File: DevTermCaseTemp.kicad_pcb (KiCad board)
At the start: 2 copper layers, 98.2 x 77 mm, 1 part, among them J1 miniPCIe

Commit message: in production. good luck!
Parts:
- added C1: 10uF, Capacitor_SMD:C_0805_2012Metric, B.Cu at (106.1, 81.5)
- added C10: 1uF, Capacitor_SMD:C_0805_2012Metric, B.Cu at (135.1, 94.3)
- added C11: 100nF, Capacitor_SMD:C_0805_2012Metric, B.Cu at (133.1, 94.3)
- added C12: 20pF, Capacitor_SMD:C_0805_2012Metric, B.Cu at (139.2, 109.2)
- added C13: 20pF, Capacitor_SMD:C_0805_2012Metric, B.Cu at (139.2, 101.6)
- added C14: 100nF, Capacitor_SMD:C_0805_2012Metric, B.Cu at (170.4, 122.9)
- added C15: 100nF, Capacitor_SMD:C_0805_2012Metric, B.Cu at (128.8, 91.4)
- added C16: 100nF, Capacitor_SMD:C_0805_2012Metric, B.Cu at (150.1, 121.2)
- added C17: 100nF, Capacitor_SMD:C_0805_2012Metric, B.Cu at (158.8, 122.4)
- added C2: 1uF, Capacitor_SMD:C_0805_2012Metric, B.Cu at (141.0, 97.8)
- added C3: 100nF, Capacitor_SMD:C_0805_2012Metric, B.Cu at (125.2, 116.3)
- added C4: 10uF, Capacitor_SMD:C_0805_2012Metric, B.Cu at (111.8, 118.6)
- added C5: 10uF, Capacitor_SMD:C_0805_2012Metric, B.Cu at (122.6, 116.1)
- added C6: 100nF, Capacitor_SMD:C_0805_2012Metric, B.Cu at (124.0, 103.1)
- added C7: 100nF, Capacitor_SMD:C_0805_2012Metric, B.Cu at (124.0, 99.3)
- added C8: 100nF, Capacitor_SMD:C_0805_2012Metric, B.Cu at (129.0, 96.0)
- added C9: 1uF, Capacitor_SMD:C_0805_2012Metric, B.Cu at (127.0, 96.0)
- added D1: ESD, Diode_SMD:D_SOD-323, B.Cu at (178.7, 96.5)
- added D10: ESD, Diode_SMD:D_SOD-323, B.Cu at (183.1, 103.1)
- added D11: ESD, Diode_SMD:D_SOD-323, B.Cu at (183.2, 100.1)
- added D12: ESD, Diode_SMD:D_SOD-323, B.Cu at (109.8, 66.6)
- added D13: ESD, Diode_SMD:D_SOD-323, B.Cu at (109.8, 69.9)
- added D14: ESD, Diode_SMD:D_SOD-323, B.Cu at (166.6, 79.2)
- added D15: ESD, Diode_SMD:D_SOD-323, B.Cu at (169.2, 79.2)
- added D16: ESD, Diode_SMD:D_SOD-323, B.Cu at (111.8, 66.6)
- added D17: ESD, Diode_SMD:D_SOD-323, B.Cu at (111.8, 69.9)
- added D18: ESD, Diode_SMD:D_SOD-323, B.Cu at (164.1, 79.2)
- added D19: ESD, Diode_SMD:D_SOD-323, B.Cu at (161.5, 79.2)
- added D2: ESD, Diode_SMD:D_SOD-323, B.Cu at (175.0, 80.4)
- added D3: ESD, Diode_SMD:D_SOD-323, B.Cu at (178.7, 98.5)
- added D4: ESD, Diode_SMD:D_SOD-323, B.Cu at (174.8, 119.9)
- added D5: ESD, Diode_SMD:D_SOD-323, B.Cu at (178.7, 103.7)
- added D6: ESD, Diode_SMD:D_SOD-323, B.Cu at (174.9, 117.6)
- added D7: LED, LED_SMD:LED_0603_1608Metric, B.Cu at (172.3, 135.9)
- added D8: LED, LED_SMD:LED_0603_1608Metric, B.Cu at (168.5, 135.9)
- added D9: ESD, Diode_SMD:D_SOD-323, B.Cu at (183.2, 97.1)
- added FB1: FerriteBead, Capacitor_SMD:C_0805_2012Metric, B.Cu at (131.8, 116.1)
- added FB2: FerriteBead, Capacitor_SMD:C_0805_2012Metric, B.Cu at (124.0, 107.7)
- added H1: MountingHole_Pad, MountingHole:MountingHole_2.7mm_M2.5_DIN965_Pad, F.Cu at (147.4, 84.5)
- added H2: MountingHole_Pad, MountingHole:MountingHole_2.7mm_M2.5_DIN965_Pad, F.Cu at (172.5, 84.5)
- added H3: MountingHole_Pad, MountingHole:MountingHole_2.7mm_M2.5_DIN965_Pad, F.Cu at (172.5, 113.6)
- added J1: USB_A, Connector_USB:USB_A_CONNFLY_DS1095-WNR0, F.Cu at (179.1, 90.3)
- added J3: USB_A, Connector_USB:USB_A_CONNFLY_DS1095-WNR0, F.Cu at (179.1, 117.3)
- added J4: USB_B_Micro, Connector_USB:USB_Micro-B_Amphenol_10118194_Horizontal, B.Cu at (188.1, 100.3)
- added J5: JBAT, Connector_PinSocket_2.00mm:PinSocket_1x02_P2.00mm_Horizontal, B.Cu at (147.8, 132.2)
- added J6: Conn_01x04, Connector_PinSocket_2.00mm:PinSocket_1x04_P2.00mm_Horizontal, B.Cu at (172.9, 74.7)
- added J7: DevTermSpeaker, devterm-ext-outline:DevTerm-Speaker, F.Cu at (171.1, 126.7)
- added J8: DevTermSpeaker, devterm-ext-outline:DevTerm-Speaker, F.Cu at (116.8, 126.7)
- added J9: Conn_02x22_Odd_Even, devterm-ext-outline:C64_expansion_2x22_socket, B.Cu at (169.2, 72.1)
- added JP1: A2, Connector_PinHeader_2.54mm:PinHeader_1x03_P2.54mm_Horizontal, B.Cu at (118.6, 124.2)
- added JP2: A1, Connector_PinHeader_2.54mm:PinHeader_1x03_P2.54mm_Horizontal, B.Cu at (128.8, 124.2)
- added JP3: A0, Connector_PinHeader_2.54mm:PinHeader_1x03_P2.54mm_Horizontal, B.Cu at (138.9, 124.2)
- added R1: 30K, Resistor_SMD:R_0805_2012Metric, B.Cu at (126.2, 113.5)
- added R10: 10K, Resistor_SMD:R_0805_2012Metric, B.Cu at (113.5, 111.5)
- added R11: 6.8K/1%, Resistor_SMD:R_0805_2012Metric, B.Cu at (109.2, 114.6)
- added R12: 1K, Resistor_SMD:R_0805_2012Metric, B.Cu at (176.1, 129.3)
- added R13: 15K, Resistor_SMD:R_0805_2012Metric, B.Cu at (124.5, 91.4)
- added R14: 1K, Resistor_SMD:R_0805_2012Metric, B.Cu at (165.4, 129.3)
- added R15: 100K, Resistor_SMD:R_0805_2012Metric, B.Cu at (113.0, 123.2)
- added R16: 100K, Resistor_SMD:R_0805_2012Metric, B.Cu at (110.5, 123.2)
- added R17: 1K, Resistor_SMD:R_0805_2012Metric, B.Cu at (168.5, 131.2)
- added R18: 1K, Resistor_SMD:R_0805_2012Metric, B.Cu at (172.3, 131.2)
- added R19: 100K, Resistor_SMD:R_0805_2012Metric, B.Cu at (114.8, 78.5)
- added R2: 680R/1%, Resistor_SMD:R_0805_2012Metric, B.Cu at (131.8, 113.3)
- added R3: 100K, Resistor_SMD:R_0805_2012Metric, B.Cu at (138.6, 94.2)
- added R4: 10K, Resistor_SMD:R_0805_2012Metric, B.Cu at (140.6, 94.2)
- added R5: 10K, Resistor_SMD:R_0805_2012Metric, B.Cu at (107.2, 73.7)
- added R6: 100K, Resistor_SMD:R_0805_2012Metric, B.Cu at (130.3, 111.3)
- added R7: 6.8K/1%, Resistor_SMD:R_0805_2012Metric, B.Cu at (104.0, 77.9)
- added R8: 47K, Resistor_SMD:R_0805_2012Metric, B.Cu at (134.6, 97.9)
- added R9: 30K, Resistor_SMD:R_0805_2012Metric, B.Cu at (129.8, 116.1)
- added REF**: mpcie-silk-back, devterm-ext-outline:mpcie-silk-back, B.Cu at (94.3, 98.0)
- added REF**: turbo_fan_3505, devterm-ext-outline:turbo_fan_3505, B.Cu at (180.0, 99.1)
- added SW1: SW_DIP_x02, Button_Switch_SMD:SW_DIP_SPSTx02_Slide_6.7x6.64mm_W6.73mm_P2.54mm_LowProfile_JPin, B.Cu at (112.0, 129.8)
- added U1: GL850G, GL850G:SSOP28, B.Cu at (130.6, 105.7)
- added U10: 4052, Package_SO:SOIC-16_3.9x9.9mm_P1.27mm, B.Cu at (104.9, 95.2)
- added U11: 4052, Package_SO:SOIC-16_3.9x9.9mm_P1.27mm, B.Cu at (118.1, 95.2)
- added U12: TXS0102DCU, Package_SO:VSSOP-8_2.3x2mm_P0.5mm, B.Cu at (153.9, 120.4)
- added U2: SY6280, SY6280:SOT23-5P95_285X100L45X40N, B.Cu at (107.5, 77.6)
- added U3: SY6280, SY6280:SOT23-5P95_285X100L45X40N, B.Cu at (113.3, 114.8)
- added U4: DS1307+, devterm-ext-outline:SOIC-8, B.Cu at (154.7, 129.3)
- added U5: MCP23008-xSS, Package_SO:SOIC-20W_7.5x12.8mm_P1.27mm, B.Cu at (130.3, 83.3)
- added U6: CH340N, Package_SO:SOP-8_3.9x4.9mm_P1.27mm, B.Cu at (170.4, 126.7)
- added U7: 4052, Package_SO:SOIC-16_3.9x9.9mm_P1.27mm, B.Cu at (138.2, 116.8)
- added U8: 4052, Package_SO:SOIC-16_3.9x9.9mm_P1.27mm, B.Cu at (104.9, 107.2)
- added U9: gp7101, Package_SO:SOP-8_3.9x4.9mm_P1.27mm, B.Cu at (185.9, 75.2)
- added Y1: 12MHz, Crystal:Crystal_SMD_3225-4Pin_3.2x2.5mm_HandSoldering, B.Cu at (139.2, 105.4)
- added Y2: 32.768KHz, Crystal:Crystal_DS26_D2.0mm_L6.0mm_Horizontal, B.Cu at (158.8, 132.3)
- J2: renamed from J1; value miniPCIe -> EXT_miniPCIe
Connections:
- net /CAM_D2_N renamed /CAM2.D-
- net /CAM_D2_P renamed /CAM2.D+
- net /CAM_D3_N renamed /CAM3.D-
- net /CAM_D3_P renamed /CAM3.D+
- J2 pad 13: /USB4_D_P -> /USB4.D+
- J2 pad 15: /USB4_D_N -> /USB4.D-
- J2 pad 17: unconnected-(J1-Pad17) -> +3.3V
- J2 pad 19: unconnected-(J1-Pad19) -> +3.3V
- J2 pad 35: /CAM_C_P -> /CAM.C+
- J2 pad 37: /CAM_C_N -> /CAM.C-
- J2 pad 41: /CAM_D1_P -> /CAM1.D+
- J2 pad 43: /CAM_D1_N -> /CAM1.D-
- J2 pad 45: unconnected-(J1-Pad45) -> GND
- J2 pad 47: unconnected-(J1-Pad47) -> /CAM0.D+
- J2 pad 49: unconnected-(J1-Pad49) -> /CAM0.D-
- J2 pad 51: unconnected-(J1-Pad51) -> GND
- J2 pad 7: /USB3_D_P -> /USB3.D+
- J2 pad 9: /USB3_D_N -> /USB3.D-
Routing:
- net GND: track 0.00 -> 436.3 mm, vias 0 -> 54
- net +5V: track 0.00 -> 327.8 mm, vias 0 -> 12
- net /UART_TX: track 0.00 -> 205.6 mm, vias 0 -> 5
- net +5VP: track 0.00 -> 204.7 mm, vias 0 -> 6
- net /UART_RX: track 0.00 -> 199.6 mm, vias 0 -> 4
- net +3.3V: track 0.00 -> 188.0 mm, vias 0 -> 8
- net /IO43: track 0.00 -> 174.6 mm, vias 0 -> 14
- net /I2C_SCL: track 0.00 -> 135.5 mm, vias 0 -> 7
- net +3.3VP: track 0.00 -> 133.4 mm, vias 0 -> 3
- net /I2C_SDA: track 0.00 -> 132.1 mm, vias 0 -> 7
- net /SPK_LN: track 0.00 -> 130.1 mm, vias 0 -> 1
- net /IO28: track 0.00 -> 123.1 mm, vias 0 -> 3
- net /IO44: track 0.00 -> 119.8 mm, vias 0 -> 6
- net /IO29: track 0.00 -> 117.9 mm, vias 0 -> 2
- net /IO45: track 0.00 -> 116.3 mm, vias 0 -> 7
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- added copper zone on B.Cu, net GND
- added copper zone on F.Cu, net GND
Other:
- board text added: "16"
- board text added: "18"
- board text added: "2"
- board text added: "52"

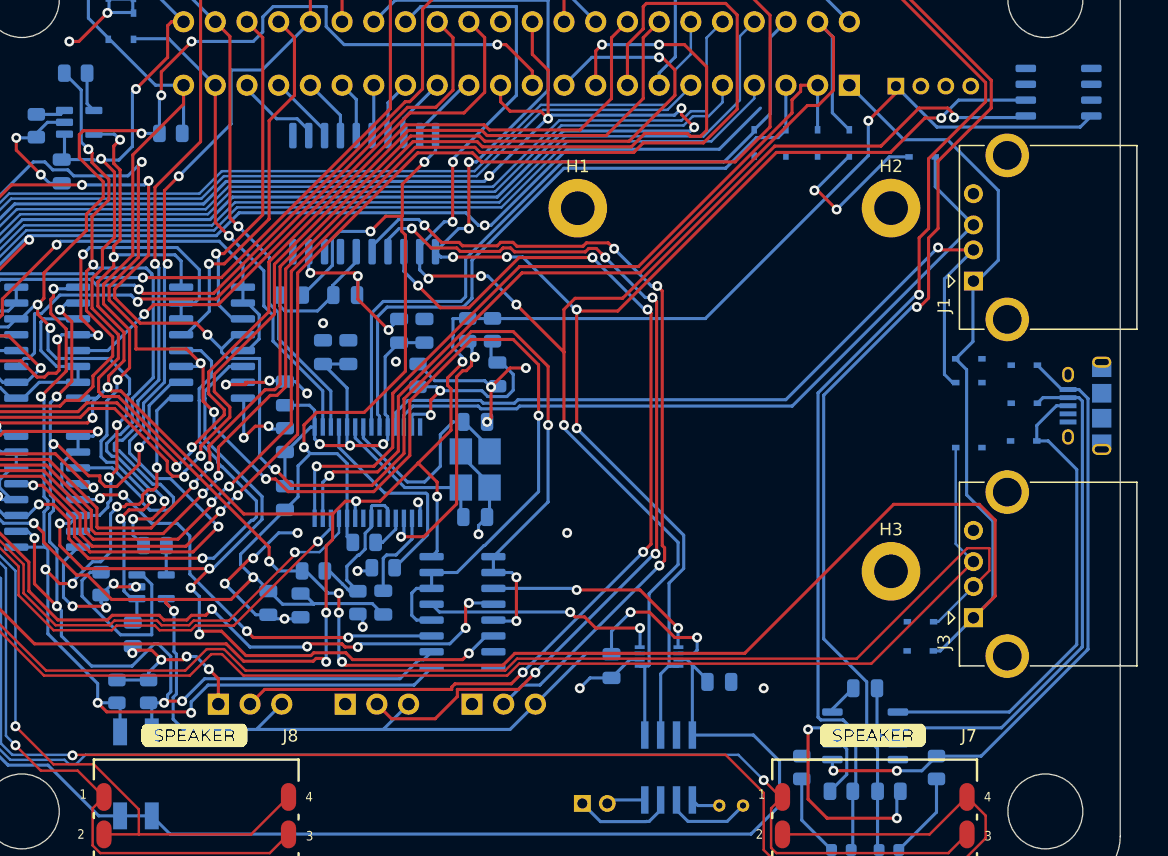
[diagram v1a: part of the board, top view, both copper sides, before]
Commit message: i2c level shifter to ssop
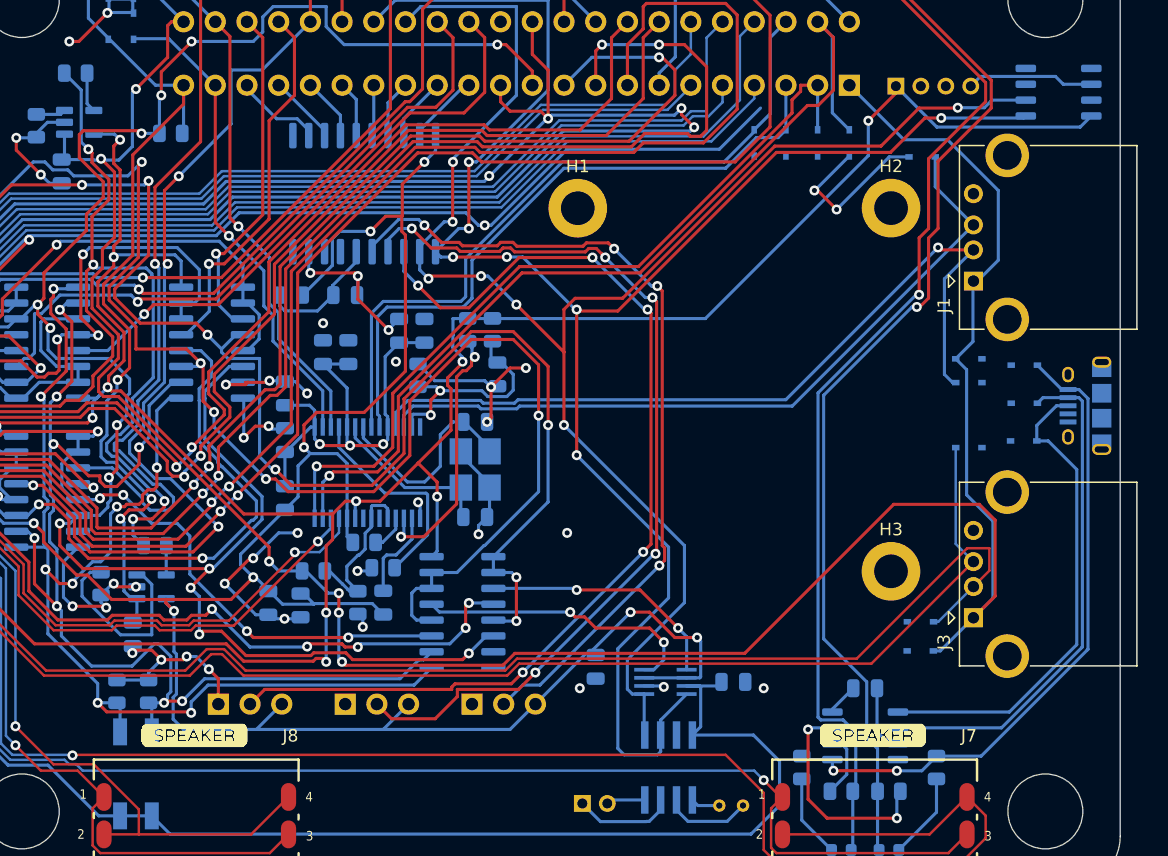
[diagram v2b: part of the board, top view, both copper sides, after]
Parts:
- U12: value TXS0102DCU -> TXS0102DCT; footprint Package_SO:VSSOP-8_2.3x2mm_P0.5mm -> Package_SO:SSOP-8_2.95x2.8mm_P0.65mm
- moved U12 2.09 mm to (154.4, 122.4)
- moved C16 1.27 mm to (148.8, 121.2)
- moved C17 1.13 mm to (159.9, 122.4)
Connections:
- J6 pad 4: GND -> Net-(J6-Pad4)
- U9 pad 1: /I2C_SDA -> /I2C_SCL
- U9 pad 2: /I2C_SCL -> /I2C_SDA
- U9 pad 6: GND -> Net-(J6-Pad4)
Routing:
- net Net-(J6-Pad4): track 0.00 -> 10.2 mm
- net /I2C_SCL: track 135.5 -> 144.2 mm
- net GND: track 436.3 -> 432.1 mm, vias 54 -> 55
- net Net-(U7-Pad13): track 19.0 -> 23.2 mm
- net Net-(U7-Pad3): track 17.6 -> 19.7 mm
- net +3.3V: track 188.0 -> 189.3 mm
- net /I2C_SDA: track 132.1 -> 133.2 mm
- net /SPK_LP: track 109.5 -> 108.9 mm
